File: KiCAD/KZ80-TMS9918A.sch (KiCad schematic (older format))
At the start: 38 parts, among them J1 Conn_Coaxial, J2 SBC8080 BUS, J3 EXT_JP, J4 AD_JP, J5 AD_JP, Q1 2SC1815, U1 74HCT04, U2 74HC139, U3 74HC32, U4 TMS9918A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

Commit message: RCAコネクタフットプリント作成。出力回路見直し
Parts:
- removed C3: 0.1U, Capacitor_THT:C_Disc_D3.0mm_W1.6mm_P2.50mm, symbol Device:C
- added C14: 0.1u, Capacitor_THT:C_Disc_D3.0mm_W1.6mm_P2.50mm, symbol Device:C
- added C15: 470u, Capacitor_THT:CP_Radial_D8.0mm_P3.50mm, symbol Device:CP
- added C3: 10u, Capacitor_THT:CP_Radial_D5.0mm_P2.50mm, symbol Device:CP
- added R4: 75, Resistor_THT:R_Axial_DIN0207_L6.3mm_D2.5mm_P10.16mm_Horizontal, symbol Device:R_US
- added R5: 10k, Resistor_THT:R_Axial_DIN0207_L6.3mm_D2.5mm_P10.16mm_Horizontal, symbol Device:R_US
- J1: footprint Connector_Coaxial:SMA_Molex_73251-1153_EdgeMount_Horizontal -> RCACon:RCAConAE
- J4, J5: symbol Connector_Generic:Conn_02x04_Counter_Clockwise -> Connector_Generic:Conn_02x04_Odd_Even
- R1: value 75 -> 300
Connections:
- wire segments 346 -> 356
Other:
- moved on the sheet: J1, L1
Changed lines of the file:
@@
 R~W
 Text Label 1400 1300 0    50   ~ 0
+D7
+Text Label 1400 1400 0    50   ~ 0
+D6
+Text Label 1400 1500 0    50   ~ 0
+D5
+Text Label 1400 1600 0    50   ~ 0
+D4
+Text Label 1400 1700 0    50   ~ 0
+D3
+Text Label 1400 1800 0    50   ~ 0
+D2
+Text Label 1400 1900 0    50   ~ 0
+D1
+Text Label 1400 2000 0    50   ~ 0
 D0
-Text Label 1400 1400 0    50   ~ 0
-D1
-Text Label 1400 1500 0    50   ~ 0
-D2
-Text Label 1400 1600 0    50   ~ 0
-D3
-Text Label 1400 1700 0    50   ~ 0
-D4
-Text Label 1400 1800 0    50   ~ 0
-D5
-Text Label 1400 1900 0    50   ~ 0
-D6
-Text Label 1400 2000 0    50   ~ 0
-D7
 $Comp
 L 74xx:74HCT04 U1
@@
 CLK
 $Comp
-L Transistor_BJT:2SC1815 Q1
-U 1 1 5D47CA6E
-P 2500 5100
-F 0 "Q1" H 2350 5250 50  0000 L CNN
-F 1 "2SC1815" H 2100 4950 50  0000 L CNN
-F 2 "Package_TO_SOT_THT:TO-92_Inline_Wide" H 2700 5025 50  0001 L CIN
-F 3 "https://media.digikey.com/pdf/Data%20Sheets/Toshiba%20PDFs/2SC1815.pdf" H 2500 5100 50  0001 L CNN
-	1    2500 5100
-	-1   0    0    -1
-$EndComp
-$Comp
 L Device:R_US R2
 U 1 1 5D48A6FF
@@
 L power:VCC #PWR06
 U 1 1 5D4A6A34
-P 1850 4300
-F 0 "#PWR06" H 1850 4150 50  0001 C CNN
-F 1 "VCC" H 1867 4473 50  0000 C CNN
-F 2 "" H 1850 4300 50  0001 C CNN
-F 3 "" H 1850 4300 50  0001 C CNN
-	1    1850 4300
-	1    0    0    -1
-$EndComp
-$Comp
-L Device:C C3
-U 1 1 5D4A6A5F
-P 1850 5050
-F 0 "C3" H 1965 5096 50  0000 L CNN
-F 1 "0.1U" H 1650 4950 50  0000 L CNN
-F 2 "Capacitor_THT:C_Disc_D3.0mm_W1.6mm_P2.50mm" H 1888 4900 50  0001 C CNN
-F 3 "~" H 1850 5050 50  0001 C CNN
-	1    1850 5050
+P 750 4300
+F 0 "#PWR06" H 750 4150 50  0001 C CNN
+F 1 "VCC" H 767 4473 50  0000 C CNN
+F 2 "" H 750 4300 50  0001 C CNN
+F 3 "" H 750 4300 50  0001 C CNN
+	1    750  4300
 	1    0    0    -1
 $EndComp
@@
 L Device:L_Core_Ferrite L1
 U 1 1 5D4A7380
-P 1850 4550
-F 0 "L1" H 1938 4596 50  0000 L CNN
-F 1 "L_Core_Ferrite" H 1938 4505 50  0000 L CNN
-F 2 "Inductor_THT:L_Axial_L5.3mm_D2.2mm_P10.16mm_Horizontal_Vishay_IM-1" H 1850 4550 50  0001 C CNN
-F 3 "~" H 1850 4550 50  0001 C CNN
-	1    1850 4550
-	1    0    0    -1
-$EndComp
-Wire Wire Line
-	1850 4300 1850 4400
-Wire Wire Line
-	1850 4700 1850 4800
-Wire Wire Line
-	1850 4800 2400 4800
+P 750 4550
+F 0 "L1" H 838 4596 50  0000 L CNN
+F 1 "L_Core_Ferrite" H 838 4505 50  0000 L CNN
+F 2 "Inductor_THT:L_Axial_L5.3mm_D2.2mm_P10.16mm_Horizontal_Vishay_IM-1" H 750 4550 50  0001 C CNN
+F 3 "~" H 750 4550 50  0001 C CNN
+	1    750  4550
+	1    0    0    -1
+$EndComp
+Wire Wire Line
+	750  4300 750  4400
+Wire Wire Line
+	750  4700 750  4800
+Wire Wire Line
+	750  4800 950  4800
 Wire Wire Line
 	2400 4800 2400 4900
-Connection ~ 1850 4800
-Wire Wire Line
-	1850 4800 1850 4900
+Connection ~ 750  4800
+Wire Wire Line
+	750  4800 750  5100
 $Comp
 L Connector:Conn_Coaxial J1
 U 1 1 5D4FC86A
-P 2150 5400
-F 0 "J1" H 2150 5500 50  0000 C CNN
-F 1 "Conn_Coaxial" V 2300 5300 50  0000 C CNN
-F 2 "Connector_Coaxial:SMA_Molex_73251-1153_EdgeMount_Horizontal" H 2150 5400 50  0001 C CNN
-F 3 " ~" H 2150 5400 50  0001 C CNN
-	1    2150 5400
+P 1300 5400
+F 0 "J1" H 1300 5500 50  0000 C CNN
+F 1 "Conn_Coaxial" H 1300 5650 50  0000 C CNN
+F 2 "RCACon:RCAConAE" H 1300 5400 50  0001 C CNN
+F 3 " ~" H 1300 5400 50  0001 C CNN
+	1    1300 5400
 	-1   0    0    -1
 $EndComp
@@
 P 2400 5650
 F 0 "R1" H 2468 5696 50  0000 L CNN
-F 1 "75" H 2468 5605 50  0000 L CNN
+F 1 "300" H 2468 5605 50  0000 L CNN
 F 2 "Resistor_THT:R_Axial_DIN0207_L6.3mm_D2.5mm_P10.16mm_Horizontal" V 2440 5640 50  0001 C CNN
 F 3 "~" H 2400 5650 50  0001 C CNN
@@
 $EndComp
 Wire Wire Line
-	1850 5200 1850 5850
-Wire Wire Line
-	1850 5850 2150 5850
+	750  5400 750  5850
 Wire Wire Line
 	3100 5850 3100 5750
 Wire Wire Line
 	3100 5450 3100 5100
-Wire Wire Line
-	2400 5300 2400 5400
-Wire Wire Line
-	2400 5400 2350 5400
-Wire Wire Line
-	2400 5400 2400 5500
-Connection ~ 2400 5400
 Wire Wire Line
 	2400 5800 2400 5850
@@
 Connection ~ 3100 5100
 Wire Wire Line
-	2150 5600 2150 5850
-Connection ~ 2150 5850
-Wire Wire Line
-	2150 5850 2400 5850
+	1300 5600 1300 5850
+Connection ~ 1300 5850
 $Comp
 L 74xx:74HCT04 U1
@@
 A6
 $Comp
-L Connector_Generic:Conn_02x04_Counter_Clockwise J5
+L Connector_Generic:Conn_02x04_Odd_Even J5
 U 1 1 5DA3D4AE
 P 10700 1800
@@
 Connection ~ 11100 1700
 $Comp
-L Connector_Generic:Conn_02x04_Counter_Clockwise J4
+L Connector_Generic:Conn_02x04_Odd_Even J4
 U 1 1 5DB39F95
 P 10700 900
@@
 Wire Wire Line
 	3450 5450 3650 5450
+Wire Wire Line
+	2400 5300 2400 5400
+$Comp
+L Device:CP C15
+U 1 1 5D6598DA
+P 2150 5400
+F 0 "C15" V 1895 5400 50  0000 C CNN
+F 1 "470u" V 1986 5400 50  0000 C CNN
+F 2 "Capacitor_THT:CP_Radial_D8.0mm_P3.50mm" H 2188 5250 50  0001 C CNN
+F 3 "~" H 2150 5400 50  0001 C CNN
+	1    2150 5400
+	0    1    1    0
+$EndComp
+Wire Wire Line
+	2300 5400 2400 5400
+Connection ~ 2400 5400
+Wire Wire Line
+	2400 5400 2400 5500
+$Comp
+L Device:R_US R5
+U 1 1 5D6A37A5
+P 1950 5600
+F 0 "R5" H 2018 5646 50  0000 L CNN
+F 1 "10k" H 2018 5555 50  0000 L CNN
+F 2 "Resistor_THT:R_Axial_DIN0207_L6.3mm_D2.5mm_P10.16mm_Horizontal" V 1990 5590 50  0001 C CNN
+F 3 "~" H 1950 5600 50  0001 C CNN
+	1    1950 5600
+	1    0    0    -1
+$EndComp
+$Comp
+L Device:R_US R4
+U 1 1 5D714369
+P 1750 5400
+F 0 "R4" V 1900 5400 50  0000 L CNN
+F 1 "75" V 1818 5355 50  0000 L CNN
+F 2 "Resistor_THT:R_Axial_DIN0207_L6.3mm_D2.5mm_P10.16mm_Horizontal" V 1790 5390 50  0001 C CNN
+F 3 "~" H 1750 5400 50  0001 C CNN
+	1    1750 5400
+	0    -1   -1   0
+$EndComp
+Wire Wire Line
+	2000 5400 1950 5400
+$Comp
+L Device:C C14
+U 1 1 5D7ADB17
+P 950 5500
+F 0 "C14" H 1050 5600 50  0000 L CNN
+F 1 "0.1u" H 750 5400 50  0000 L CNN
+F 2 "Capacitor_THT:C_Disc_D3.0mm_W1.6mm_P2.50mm" H 988 5350 50  0001 C CNN
+F 3 "~" H 950 5500 50  0001 C CNN
+	1    950  5500
+	1    0    0    -1
+$EndComp
+Wire Wire Line
+	950  4800 950  5350
+Connection ~ 950  4800
+Wire Wire Line
+	950  4800 2400 4800
+Wire Wire Line
+	950  5650 950  5850
+Wire Wire Line
+	750  5850 950  5850
+Connection ~ 950  5850
+Wire Wire Line
+	950  5850 1300 5850
+Wire Wire Line
+	1500 5400 1600 5400
+Wire Wire Line
+	1300 5850 1950 5850
+Wire Wire Line
+	1950 5400 1950 5450
+Connection ~ 1950 5400
+Wire Wire Line
+	1950 5400 1900 5400
+Wire Wire Line
+	1950 5750 1950 5850
+Connection ~ 1950 5850
+Wire Wire Line
+	1950 5850 2400 5850
+$Comp
+L Transistor_BJT:2SC1815 Q1
+U 1 1 5D36B1EA
+P 2500 5100
+F 0 "Q1" H 2691 5146 50  0000 L CNN
+F 1 "2SC1815" H 2150 4950 50  0000 L CNN
+F 2 "Package_TO_SOT_THT:TO-92_Inline_Wide" H 2700 5025 50  0001 L CIN
+F 3 "https://media.digikey.com/pdf/Data%20Sheets/Toshiba%20PDFs/2SC1815.pdf" H 2500 5100 50  0001 L CNN
+	1    2500 5100
+	-1   0    0    -1
+$EndComp
+$Comp
+L Device:CP C3
+U 1 1 5D393963
+P 750 5250
+F 0 "C3" H 800 5350 50  0000 L CNN
+F 1 "10u" H 600 5150 50  0000 L CNN
+F 2 "Capacitor_THT:CP_Radial_D5.0mm_P2.50mm" H 788 5100 50  0001 C CNN
+F 3 "~" H 750 5250 50  0001 C CNN
+	1    750  5250
+	1    0    0    -1
+$EndComp
 Wire Bus Line
 	8850 600  8850 1650
@@
 	9350 3750 9350 5150
 Wire Bus Line
-	7650 3850 7650 5150
+	7650 600  7650 2150
+Wire Bus Line
+	1200 850  1200 2300
+Wire Bus Line
+	3500 700  3500 3250
+Wire Bus Line
+	7350 700  7350 1900
+Wire Bus Line
+	3300 1400 3300 3850
+Wire Bus Line
+	3300 3850 3300 5150
+Wire Bus Line
+	5000 700  5000 5150
 Wire Bus Line
 	5400 3850 5400 5150
 Wire Bus Line
-	5000 700  5000 5150
-Wire Bus Line
-	3300 3850 3300 5150
-Wire Bus Line
-	3300 1400 3300 3850
-Wire Bus Line
-	7350 700  7350 1900
-Wire Bus Line
-	3500 700  3500 3250
-Wire Bus Line
-	1200 850  1200 2300
-Wire Bus Line
-	7650 600  7650 2150
+	7650 3850 7650 5150
 Wire Bus Line
 	5450 1400 5450 3750

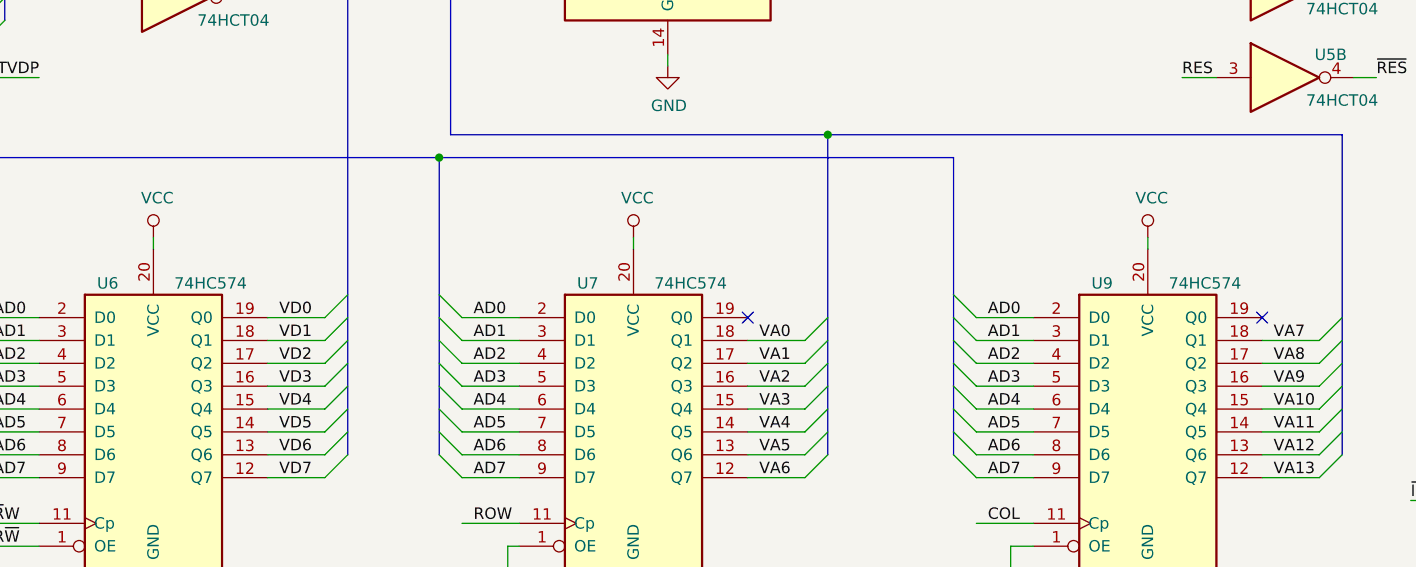
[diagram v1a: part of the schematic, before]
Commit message: 回路図表記間違い修正 74HC574→74HCT574
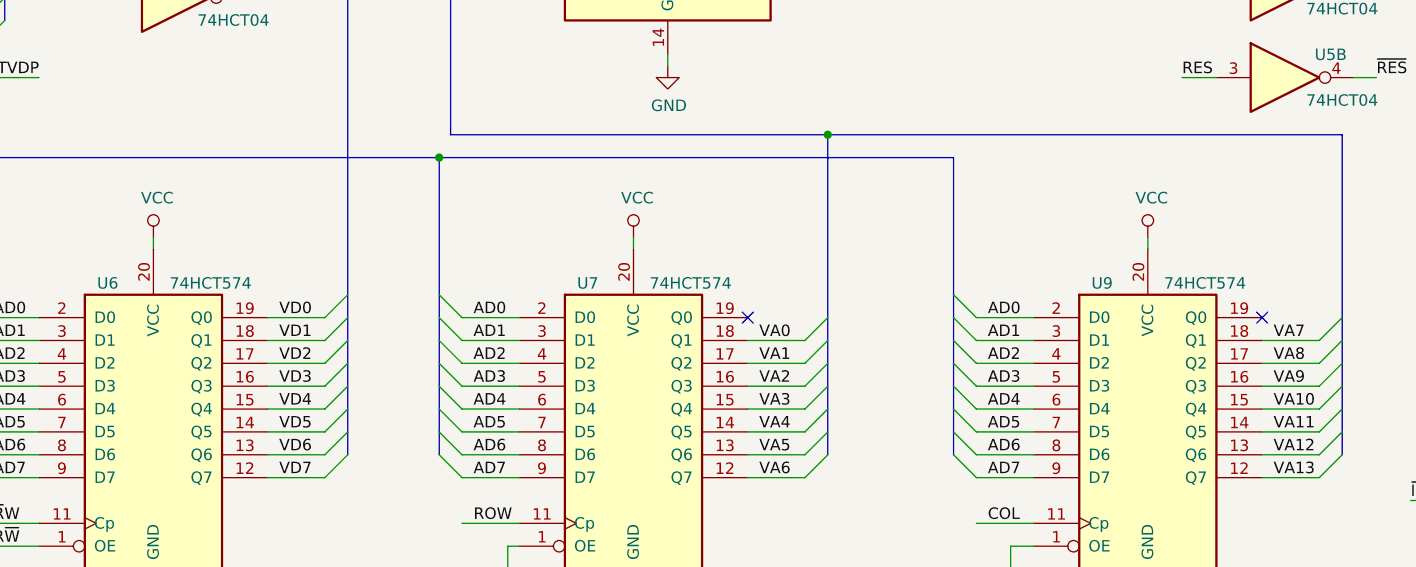
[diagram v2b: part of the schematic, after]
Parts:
- U6, U7, U9: value 74HC574 -> 74HCT574
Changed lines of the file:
@@
 P 4150 5050
 F 0 "U6" H 3950 5700 50  0000 C CNN
-F 1 "74HC574" H 4400 5700 50  0000 C CNN
+F 1 "74HCT574" H 4400 5700 50  0000 C CNN
 F 2 "Package_DIP:DIP-20_W7.62mm_Socket" H 4150 5050 50  0001 C CNN
 F 3 "http://www.ti.com/lit/gpn/sn74LS574" H 4150 5050 50  0001 C CNN
@@
 P 6250 5050
 F 0 "U7" H 6050 5700 50  0000 C CNN
-F 1 "74HC574" H 6500 5700 50  0000 C CNN
+F 1 "74HCT574" H 6500 5700 50  0000 C CNN
 F 2 "Package_DIP:DIP-20_W7.62mm_Socket" H 6250 5050 50  0001 C CNN
 F 3 "http://www.ti.com/lit/gpn/sn74LS574" H 6250 5050 50  0001 C CNN
@@
 P 8500 5050
 F 0 "U9" H 8300 5700 50  0000 C CNN
-F 1 "74HC574" H 8750 5700 50  0000 C CNN
+F 1 "74HCT574" H 8750 5700 50  0000 C CNN
 F 2 "Package_DIP:DIP-20_W7.62mm_Socket" H 8500 5050 50  0001 C CNN
 F 3 "http://www.ti.com/lit/gpn/sn74LS574" H 8500 5050 50  0001 C CNN

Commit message: パターンチェック後 SBCバスINT修正 、製造ファイル再出力
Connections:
- net INT: no longer J2.23 (Pin_23)
- no-connect marks 25 -> 26
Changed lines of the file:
@@
 Wire Wire Line
 	8000 2050 7750 2050
-Wire Wire Line
-	8000 2150 7750 2150
 Entry Wire Line
 	7750 1850 7650 1750
@@
 Entry Wire Line
 	7750 2050 7650 1950
-Entry Wire Line
-	7750 2150 7650 2050
 Text Label 7850 1450 0    50   ~ 0
 D0
@@
 Text Label 7850 2050 0    50   ~ 0
 RES
-Text Label 7850 2150 0    50   ~ 0
-INT
 Wire Wire Line
 	8500 1450 8750 1450
@@
 	1    0    0    -1
 $EndComp
+NoConn ~ 8000 2150
 Wire Bus Line
 	8850 600  8850 1650

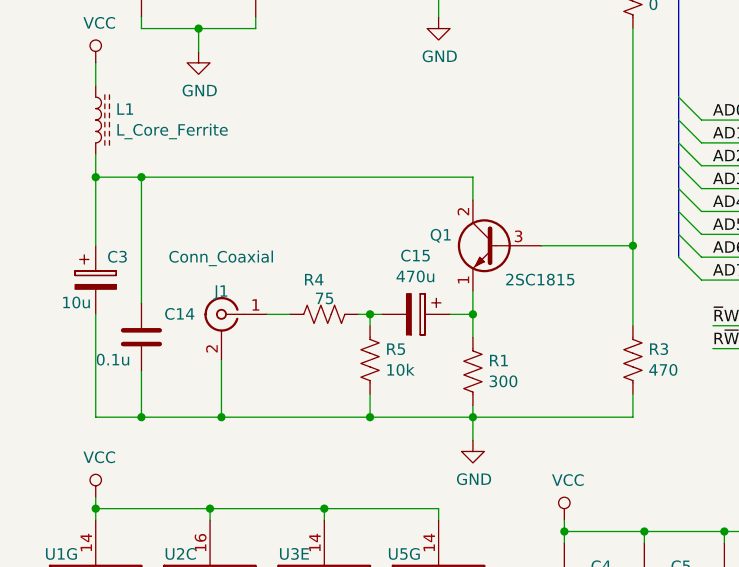
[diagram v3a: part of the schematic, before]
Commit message: 回路見直し&パターン再作成
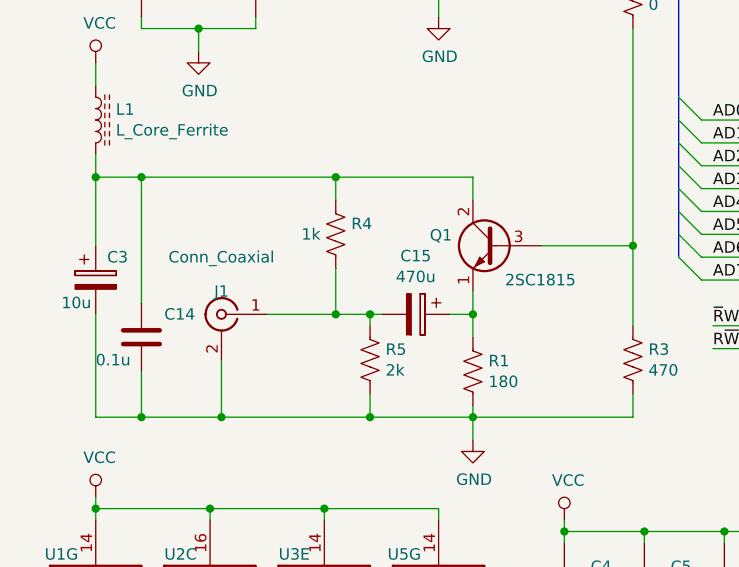
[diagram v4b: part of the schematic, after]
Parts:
- R1: value 300 -> 180
- R4: value 75 -> 1k
- R5: value 10k -> 2k
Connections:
- net at C14.1, C3.1, L1.2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: now also R4.1
- net at J1.1 (In): now also C15.2, R4.2, R5.1; no longer R4.1
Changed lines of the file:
@@
 P 2400 5650
 F 0 "R1" H 2468 5696 50  0000 L CNN
-F 1 "300" H 2468 5605 50  0000 L CNN
+F 1 "180" H 2468 5605 50  0000 L CNN
 F 2 "Resistor_THT:R_Axial_DIN0207_L6.3mm_D2.5mm_P10.16mm_Horizontal" V 2440 5640 50  0001 C CNN
 F 3 "~" H 2400 5650 50  0001 C CNN
@@
 P 1950 5600
 F 0 "R5" H 2018 5646 50  0000 L CNN
-F 1 "10k" H 2018 5555 50  0000 L CNN
+F 1 "2k" H 2018 5555 50  0000 L CNN
 F 2 "Resistor_THT:R_Axial_DIN0207_L6.3mm_D2.5mm_P10.16mm_Horizontal" V 1990 5590 50  0001 C CNN
 F 3 "~" H 1950 5600 50  0001 C CNN
@@
 	1    0    0    -1
 $EndComp
-$Comp
-L Device:R_US R4
-U 1 1 5D714369
-P 1750 5400
-F 0 "R4" V 1900 5400 50  0000 L CNN
-F 1 "75" V 1818 5355 50  0000 L CNN
-F 2 "Resistor_THT:R_Axial_DIN0207_L6.3mm_D2.5mm_P10.16mm_Horizontal" V 1790 5390 50  0001 C CNN
-F 3 "~" H 1750 5400 50  0001 C CNN
-	1    1750 5400
-	0    -1   -1   0
-$EndComp
-Wire Wire Line
-	2000 5400 1950 5400
 $Comp
 L Device:C C14
@@
 Connection ~ 950  4800
 Wire Wire Line
-	950  4800 2400 4800
+	950  4800 1800 4800
 Wire Wire Line
 	950  5650 950  5850
@@
 	950  5850 1300 5850
 Wire Wire Line
-	1500 5400 1600 5400
-Wire Wire Line
 	1300 5850 1950 5850
-Wire Wire Line
-	1950 5400 1950 5450
-Connection ~ 1950 5400
-Wire Wire Line
-	1950 5400 1900 5400
 Wire Wire Line
 	1950 5750 1950 5850
@@
 $EndComp
 NoConn ~ 8000 2150
+$Comp
+L Device:R_US R4
+U 1 1 5D316E34
+P 1800 5050
+F 0 "R4" H 1868 5096 50  0000 L CNN
+F 1 "1k" H 1650 5050 50  0000 L CNN
+F 2 "Resistor_THT:R_Axial_DIN0207_L6.3mm_D2.5mm_P10.16mm_Horizontal" V 1840 5040 50  0001 C CNN
+F 3 "~" H 1800 5050 50  0001 C CNN
+	1    1800 5050
+	1    0    0    -1
+$EndComp
+Wire Wire Line
+	1800 4900 1800 4800
+Connection ~ 1800 4800
+Wire Wire Line
+	1800 4800 2400 4800
+Wire Wire Line
+	1800 5200 1800 5400
+Wire Wire Line
+	1500 5400 1800 5400
+Wire Wire Line
+	1800 5400 1950 5400
+Connection ~ 1800 5400
+Wire Wire Line
+	1950 5400 1950 5450
+Connection ~ 1950 5400
+Wire Wire Line
+	1950 5400 2000 5400
 Wire Bus Line
 	8850 600  8850 1650

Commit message: INT端子ジャンパ装備 パターン再作成、ガーバー出力
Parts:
- added JP2: INT-J, Connector_PinHeader_2.54mm:PinHeader_1x03_P2.54mm_Vertical, symbol Jumper:Jumper_3_Open
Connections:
- net labels added: INT80
- wire segments 358 -> 360
- no-connect marks 26 -> 25
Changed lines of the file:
@@
 	10600 5350 10600 5550
-Wire Wire Line
-	10600 5550 9750 5550
-Wire Wire Line
-	9750 5550 9750 6200
 Wire Wire Line
 	9750 6200 10350 6200
@@
 	1    0    0    -1
 $EndComp
-NoConn ~ 8000 2150
 $Comp
 L Device:R_US R4
@@
 Wire Wire Line
 	1950 5400 2000 5400
+Wire Wire Line
+	8000 2150 7750 2150
+Entry Wire Line
+	7750 2150 7650 2050
+Text Label 7750 2150 0    50   ~ 0
+INT80
+$Comp
+L Jumper:Jumper_3_Open JP2
+U 1 1 5D6D7932
+P 9500 6200
+F 0 "JP2" H 9500 6332 50  0000 C CNN
+F 1 "INT-J" H 9500 6423 50  0000 C CNN
+F 2 "Connector_PinHeader_2.54mm:PinHeader_1x03_P2.54mm_Vertical" H 9500 6200 50  0001 C CNN
+F 3 "~" H 9500 6200 50  0001 C CNN
+	1    9500 6200
+	-1   0    0    1
+$EndComp
+Wire Wire Line
+	9500 5550 9500 6050
+Wire Wire Line
+	9500 5550 10600 5550
+Wire Wire Line
+	9250 6200 8950 6200
+Text Label 8950 6200 0    50   ~ 0
+INT80
 Wire Bus Line
 	8850 600  8850 1650
